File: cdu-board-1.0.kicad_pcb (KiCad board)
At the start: 2 copper layers, 53.4 x 50.9 mm, 19 parts, among them J1 Conn_01x02_Socket, J2 Conn_01x03_Socket, J3 Conn_01x02_Socket, Q1 TIP220G, Q2 TIP220G

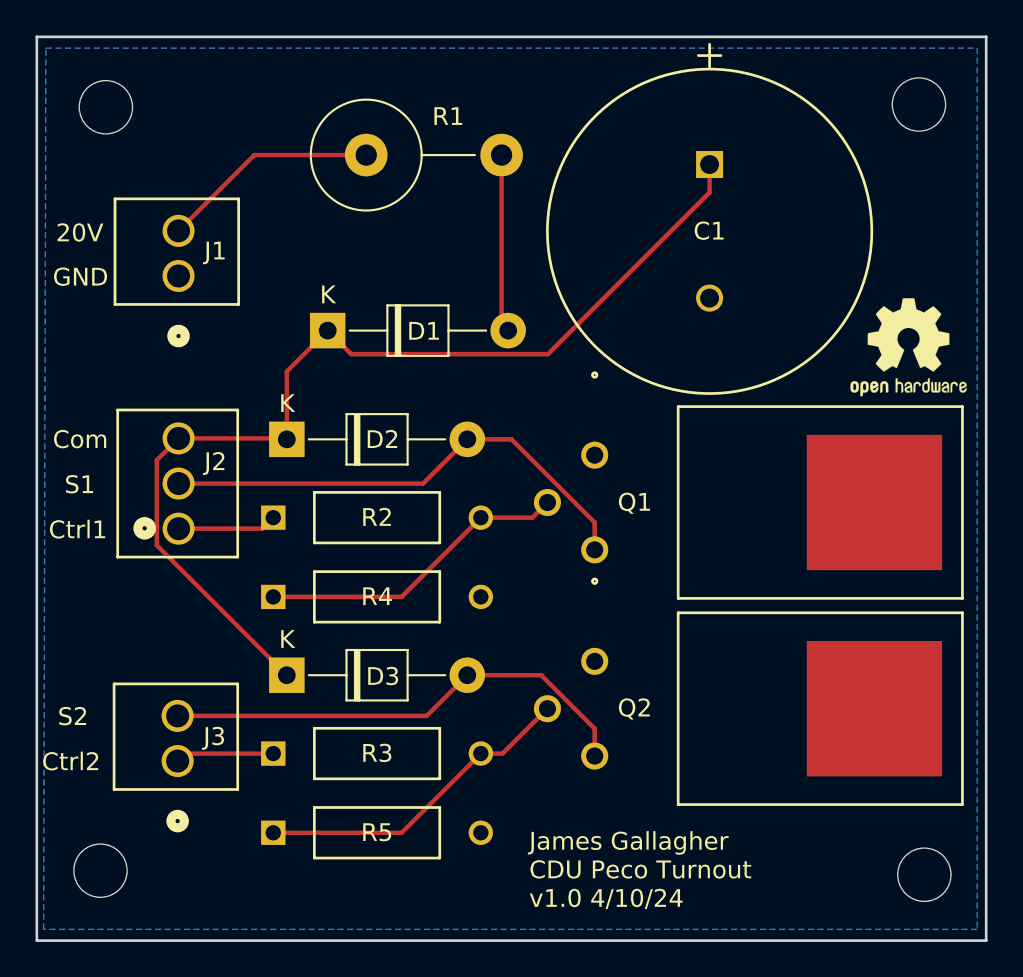
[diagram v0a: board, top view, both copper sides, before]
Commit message: Fixed transistor - v1.0 used TIP220G and not TIP120G
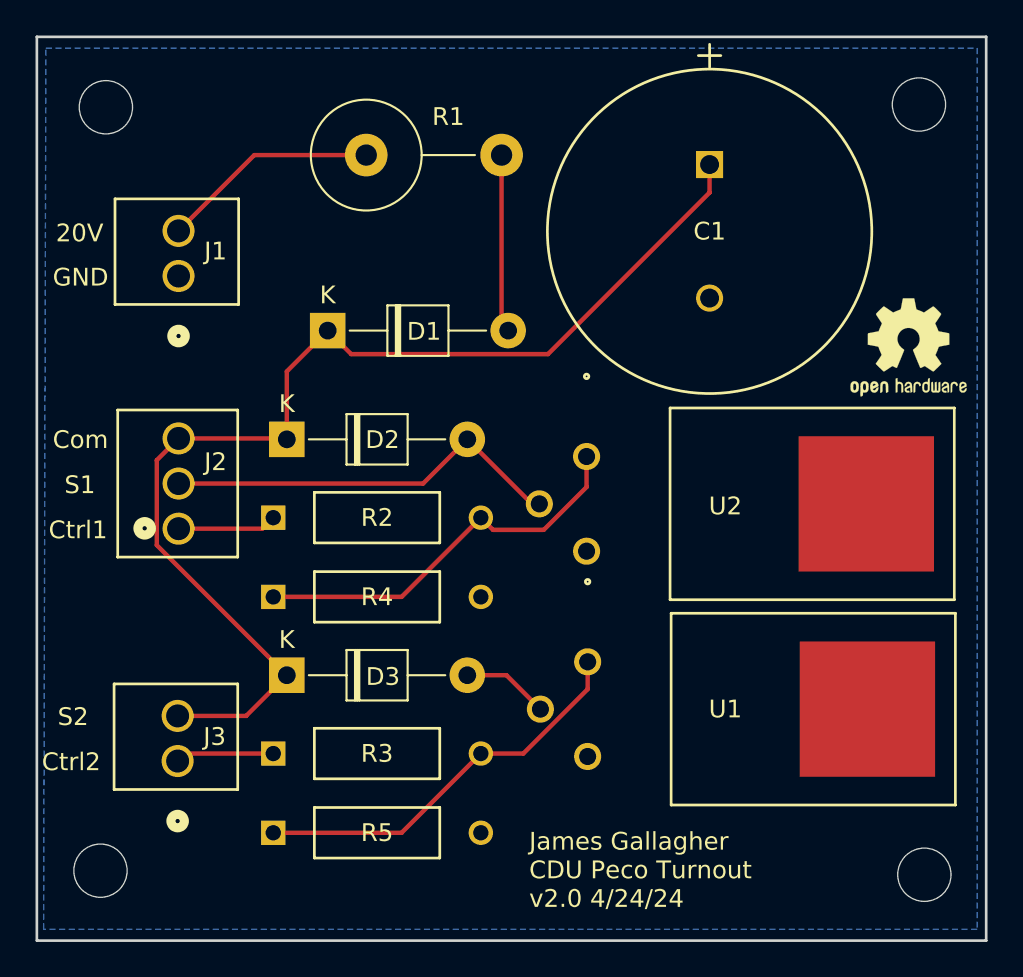
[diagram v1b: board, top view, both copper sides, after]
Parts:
- removed Q1, Q2: TIP220G, CDU footprints:TO-220-3_10P53X15P75_ONS
- added U1: TIP120G, CDU footprints:TO-220-3_10P53X15P75_ONS, F.Cu at (147.7, 113.9)
- added U2: TIP120G, CDU footprints:TO-220-3_10P53X15P75_ONS, F.Cu at (147.6, 102.4)
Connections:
- J3 pad 2: Net-(D3-A) -> Net-(D1-K)
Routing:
- net Net-(D3-A): track 27.2 -> 4.91 mm
- net Net-(D1-K): track 57.5 -> 64.5 mm
- net Net-(D2-A): track 27.9 -> 22.8 mm
- net Net-(U2-BASE): track 17.6 -> 22.5 mm
- net Net-(U1-BASE): track 18.3 -> 22.6 mm
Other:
- board text added: "James Gallagher CDU Peco Turnout v2.0 4/24/24"
- board text removed: "James Gallagher CDU Peco Turnout v1.0 4/10/24"

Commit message: Added QR code, fixed an error
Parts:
- added G***: LOGO, CDU footprints:CDU-QR, B.Cu at (159.3, 110.2)
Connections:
- J3 pad 2: Net-(D1-K) -> Net-(D3-A)
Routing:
- net Net-(D3-A): track 4.91 -> 22.2 mm
- net Net-(D1-K): track 64.5 -> 57.5 mm
